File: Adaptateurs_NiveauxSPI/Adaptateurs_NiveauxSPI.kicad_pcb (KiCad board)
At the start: 2 copper layers, 21 parts, among them P1 CONN_01X07, P2 CONN_01X08, P3 CONN_01X07, P4 CONN_01X12, P5 CONN_01X07, P6 CONN_01X09, P7 CONN_01X07, P8 CONN_01X12, U1 CON_5V_3-3V, U2 CON_5V_3-3V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

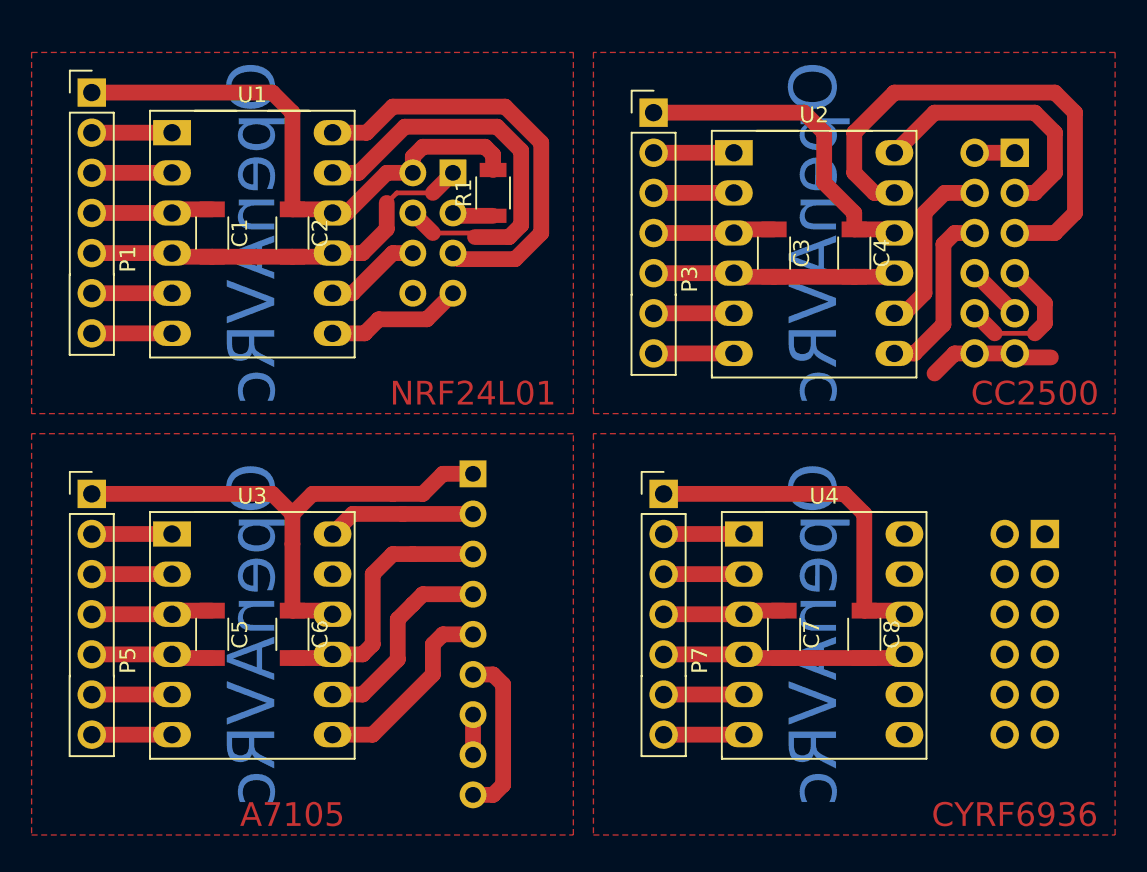
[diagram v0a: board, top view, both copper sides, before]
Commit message: Update SPI boards
- Add CYRF9636 board
- Update CC2500 board
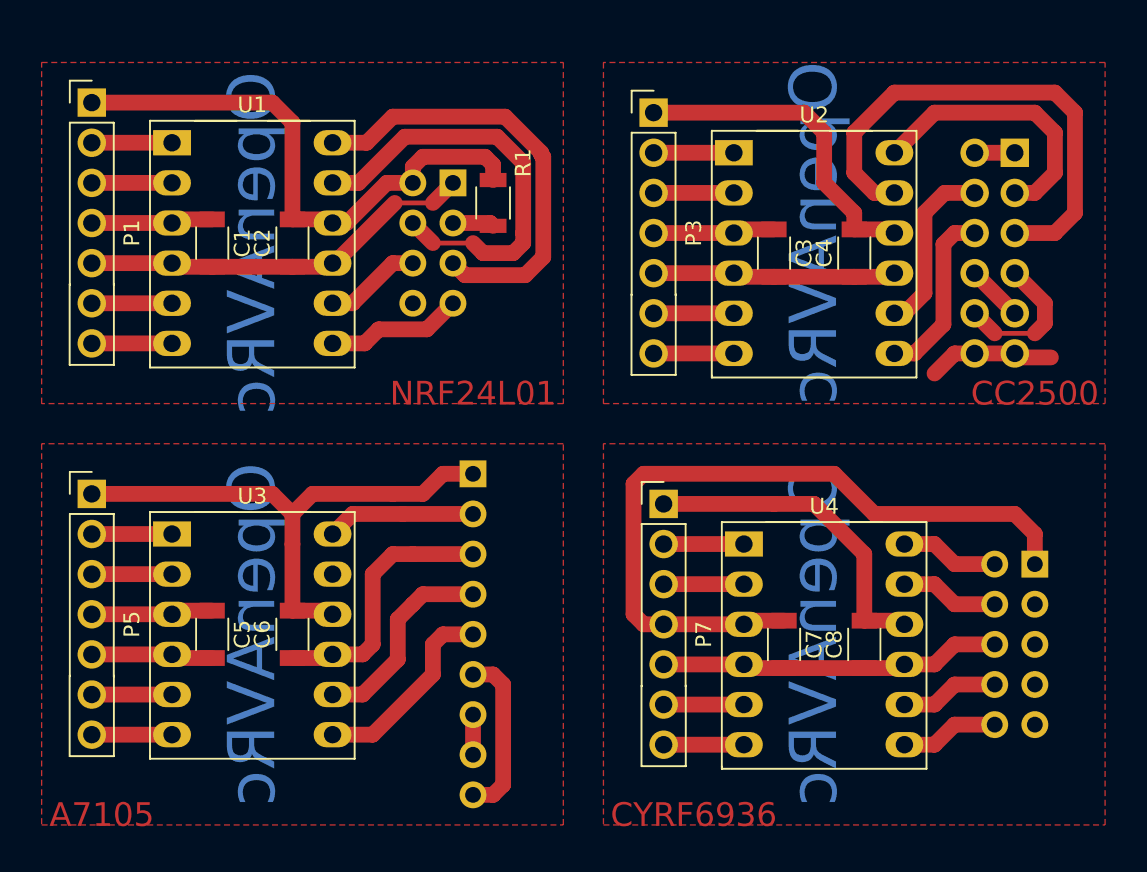
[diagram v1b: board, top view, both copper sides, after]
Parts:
- P8: value CONN_01X12 -> CONN_01X10
- moved P8 2.01 mm to (171.4, 95.9)
- moved C7 0.64 mm to (155.6, 101.0)
- moved C8 0.64 mm to (160.7, 101.0)
- moved P7 0.64 mm to (148.0, 92.1)
- moved R1 0.64 mm to (137.2, 73.0)
- moved U1 0.64 mm to (116.8, 69.2)
- moved C1 0.63 mm to (119.4, 75.6)
- moved C2 0.63 mm to (124.5, 75.6)
- moved P1 0.63 mm to (111.8, 66.7)
- moved P2 0.63 mm to (134.6, 71.8)
- moved U4 0.63 mm to (153.0, 94.6)
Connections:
- P8 pad 1: (no net) -> +5C
- P8 pad 10: (no net) -> Net-(P8-Pad10)
- P8 pad 2: (no net) -> Net-(P8-Pad2)
- P8 pad 4: (no net) -> Net-(P8-Pad4)
- P8 pad 6: (no net) -> AGND
- P8 pad 8: (no net) -> Net-(P8-Pad8)
- U4 pad 1: (no net) -> Net-(P8-Pad2)
- U4 pad 2: (no net) -> Net-(P8-Pad4)
- U4 pad 5: (no net) -> Net-(P8-Pad8)
- U4 pad 6: (no net) -> Net-(P8-Pad10)
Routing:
- net +5C: track 7.72 -> 47.3 mm
- net Net-(P8-Pad8): track 0.00 -> 6.24 mm
- net Net-(P8-Pad2): track 0.00 -> 6.24 mm
- net Net-(P8-Pad4): track 0.00 -> 6.24 mm
- net Net-(P8-Pad10): track 0.00 -> 6.24 mm
- net AGND: track 15.4 -> 21.7 mm
- net +3.3VDAC: track 22.0 -> 20.9 mm
- net Net-(P2-Pad5): track 27.0 -> 28.0 mm
- net GNDA: track 26.1 -> 25.2 mm
- net Net-(P2-Pad4): track 26.3 -> 27.1 mm
